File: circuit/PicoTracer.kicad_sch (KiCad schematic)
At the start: 19 parts, among them J1 Conn_01x04_Socket, J2 Conn_01x04_Socket, J3 Conn_01x04_Socket, J4 Conn_01x04_Socket, J5 Conn_01x04_Socket, J6 Conn_01x04_Socket, J7 8P8C, SW1 SW_Push, SW2 SW_Push, SW3 SW_Push, SW4 SW_SPDT, SW5 SW_SPDT, SW6 SW_SPDT, U1 Pico, U2 MCP3002, U3 MCP3002

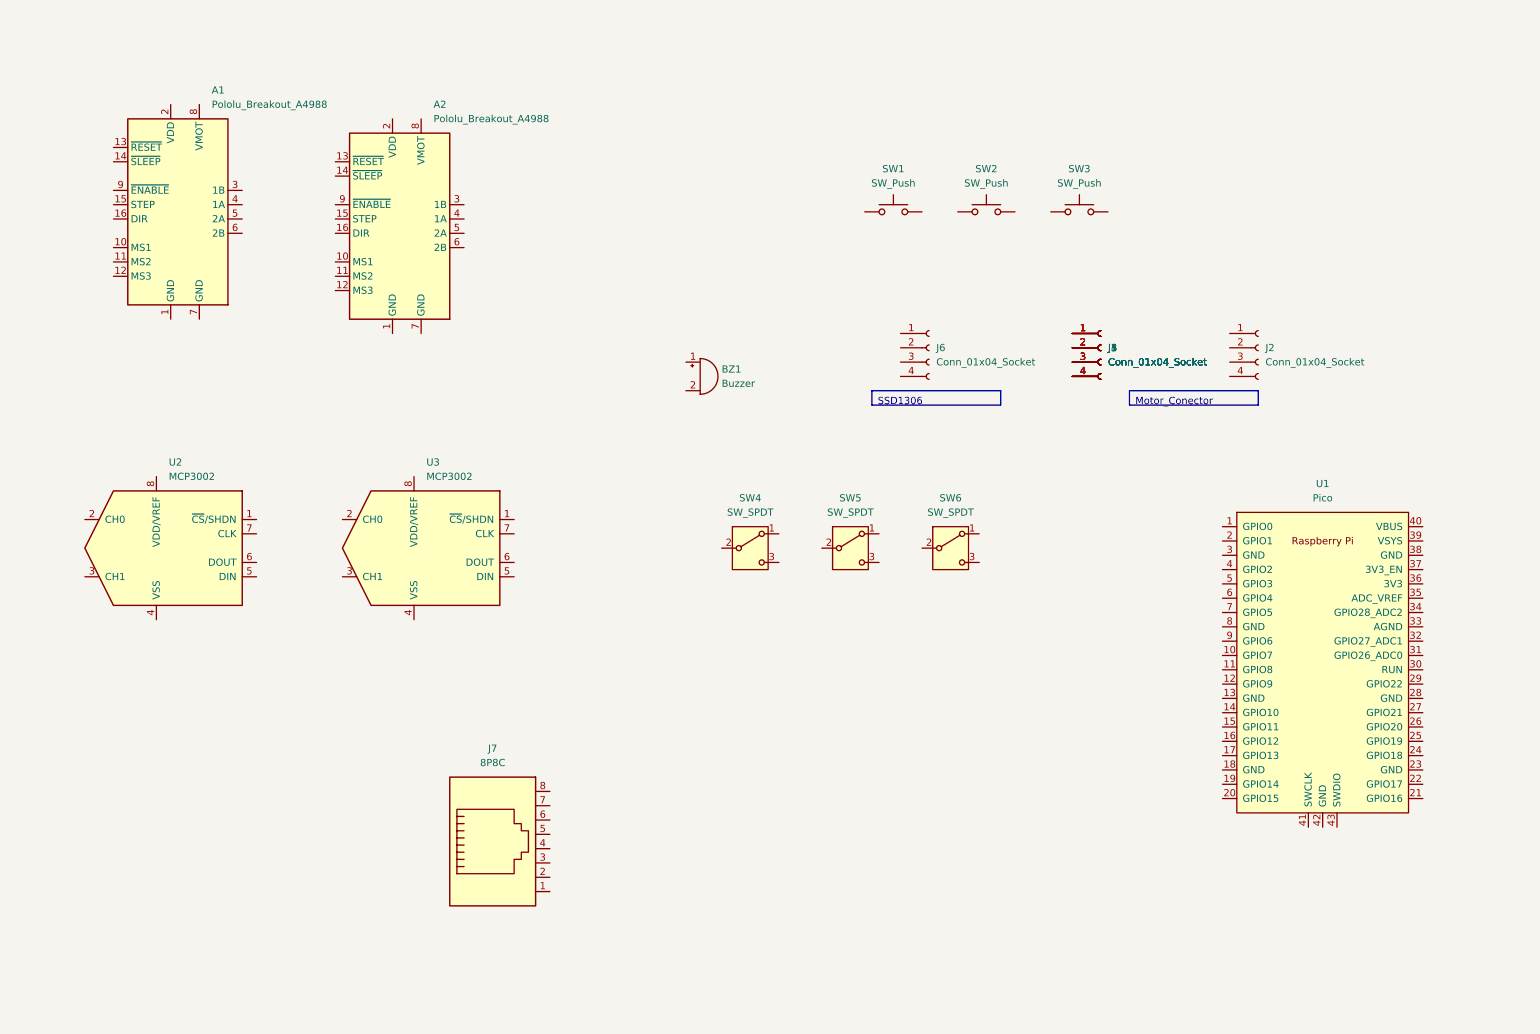
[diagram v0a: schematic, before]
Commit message: ・A4988の配線追加
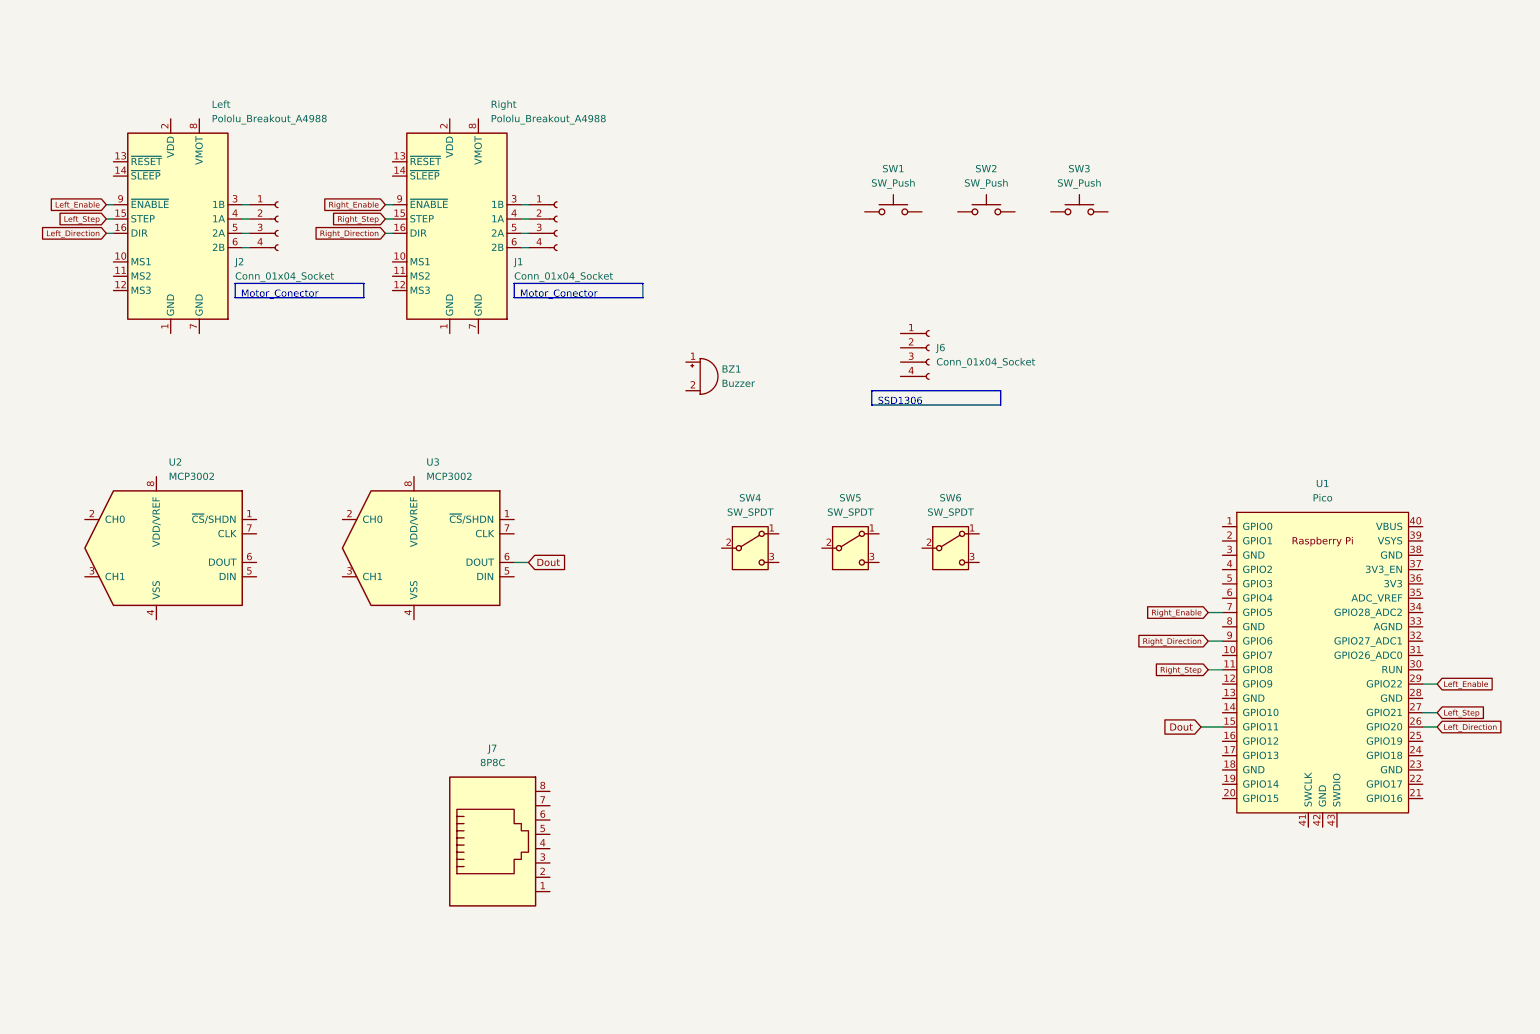
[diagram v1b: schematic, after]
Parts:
- removed J3, J4, J5: Conn_01x04_Socket, symbol Connector:Conn_01x04_Socket
- renumbered A1 to Left, A2 to Right
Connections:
- net at J1.1 (Pin_1): now also Right.3 (1B)
- net at J1.2 (Pin_2): now also Right.4 (1A)
- net at J1.3 (Pin_3): now also Right.5 (2A)
- net at J1.4 (Pin_4): now also Right.6 (2B)
- net at J2.1 (Pin_1): now also Left.3 (1B)
- net at J2.2 (Pin_2): now also Left.4 (1A)
- net at J2.3 (Pin_3): now also Left.5 (2A)
- net at J2.4 (Pin_4): now also Left.6 (2B)
- net Right_Step: now reaches U1.11 (GPIO8)
- net Right_Step: now also Right.15 (STEP)
- net Dout: now reaches U1.15 (GPIO11)
- net Dout: now also U3.6 (DOUT)
- net Left_Direction: now reaches U1.26 (GPIO20)
- net Left_Direction: now also Left.16 (DIR)
- net Left_Step: now reaches U1.27 (GPIO21)
- net Left_Step: now also Left.15 (STEP)
- net Left_Enable: now reaches U1.29 (GPIO22)
- net Left_Enable: now also Left.9 (~{ENABLE})
- net Right_Enable: now reaches U1.7 (GPIO5)
- net Right_Enable: now also Right.9 (~{ENABLE})
- net Right_Direction: now reaches U1.9 (GPIO6)
- net Right_Direction: now also Right.16 (DIR)
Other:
- moved on the sheet: J2, Left, Right

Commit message: ・スイッチ配線 ・AD変換器電源以外の配線完了
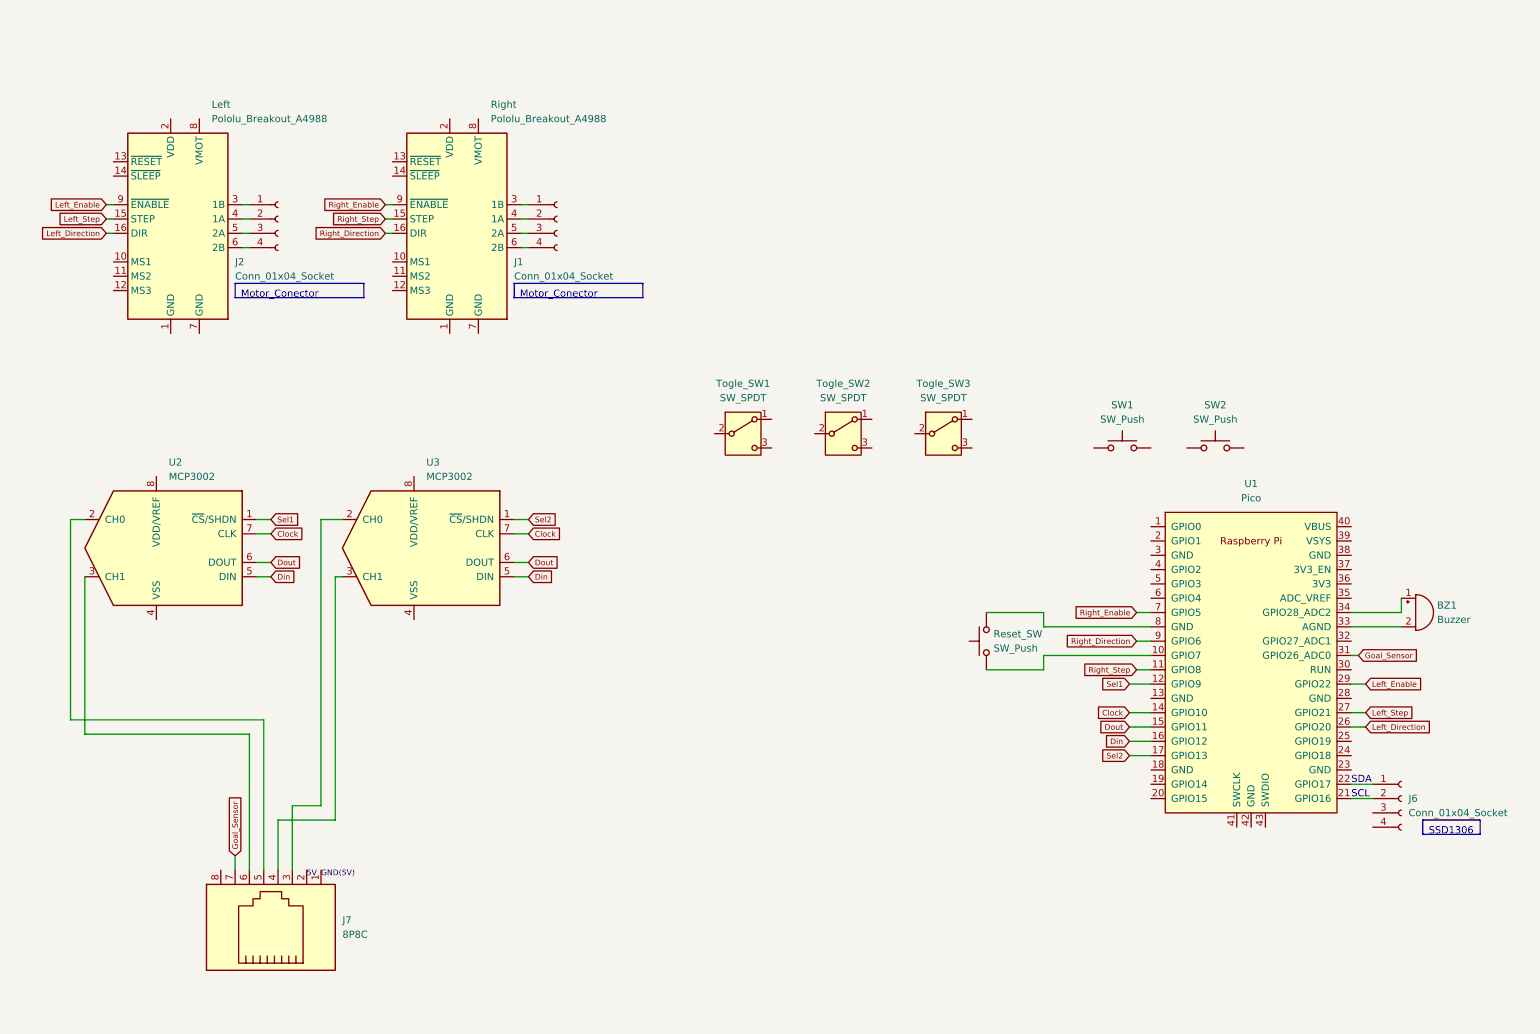
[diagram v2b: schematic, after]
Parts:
- renumbered SW3 to Reset_SW, SW4 to Togle_SW1, SW5 to Togle_SW2, SW6 to Togle_SW3
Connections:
- net Dout: now also U2.6 (DOUT)
- net at Reset_SW.1: now also U1.10 (GPIO7)
- net at Reset_SW.2: now also U1.8 (GND)
- net at J6.1 (Pin_1): now also U1.22 (GPIO17)
- net at J6.2 (Pin_2): now also U1.21 (GPIO16)
- net at J7.3: now also U3.2 (CH0)
- net at J7.4: now also U3.3 (CH1)
- net at J7.5: now also U2.2 (CH0)
- net at J7.6: now also U2.3 (CH1)
- net Goal_Sensor: now reaches J7.7
- net Goal_Sensor: now also U1.31 (GPIO26_ADC0)
- net Sel1: now reaches U2.1 (~{CS}/SHDN)
- net Sel1: now also U1.12 (GPIO9)
- net Din: now reaches U2.5 (DIN)
- net Din: now also U1.16 (GPIO12), U3.5 (DIN)
- net Clock: now reaches U2.7 (CLK)
- net Clock: now also U1.14 (GPIO10), U3.7 (CLK)
- net Sel2: now reaches U1.17 (GPIO13)
- net Sel2: now also U3.1 (~{CS}/SHDN)
- net at U1.33 (AGND): now also BZ1.2 (-)
- net at U1.34 (GPIO28_ADC2): now also BZ1.1 (+)
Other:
- note added: "5V"
- note added: "GND(5V)"
- note added: "SCL"
- note added: "SDA"
- moved on the sheet: BZ1, J6, J7, Reset_SW, SW1, SW2, Togle_SW1, Togle_SW2, Togle_SW3, U1

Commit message: scene5に電圧計測追加
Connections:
- net at Left.13 (~{RESET}): now also Left.14 (~{SLEEP})
- net at Right.13 (~{RESET}): now also Right.14 (~{SLEEP})
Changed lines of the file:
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@@
 (kicad_sch (version 20230121) (generator eeschema)
   (paper "A4")
+  (wire (pts (xy 34.29 43.18) (xy 34.29 45.72))
+    (stroke (width 0) (type default))
+  )
   (wire (pts (xy 63.5 160.02) (xy 63.5 168.91))
     (stroke (width 0) (type default))
@@
   )
   (wire (pts (xy 33.02 53.34) (xy 34.29 53.34))
+    (stroke (width 0) (type default))
+  )
+  (wire (pts (xy 83.82 43.18) (xy 83.82 45.72))
     (stroke (width 0) (type default))
   )
@@
     )
     (pin "1")
+    (pin "2")
+    (pin "3")
     (pin "4")
-    (pin "2")
-    (pin "3")
     (instances
       (project "PicoTracer"
@@
       (effects (font (size 1.27 1.27)) hide)
     )
-    (pin "2")
+    (pin "1")
+    (pin "2")
+    (pin "3")
     (pin "4")
-    (pin "3")
-    (pin "1")
     (instances
       (project "PicoTracer"
@@
       (effects (font (size 1.27 1.27)) hide)
     )
+    (pin "1")
+    (pin "2")
+    (pin "3")
+    (pin "4")
+    (pin "5")
+    (pin "6")
+    (pin "7")
     (pin "8")
+    (instances
+      (project "PicoTracer"
+        (path "/f79d951e-a1b3-4edf-883f-79f37eda87da"
+          (reference "J7") (unit 1)
+        )
+      )
+    )
+  )
+  (symbol (lib_id "Analog_ADC:MCP3002") (at 41.91 111.76 0) (unit 1)
+    (in_bom yes) (on_board yes) (dnp no) (fields_autoplaced)
+    (property "Reference" "U2" (at 44.1041 96.52 0)
+      (effects (font (size 1.27 1.27)) (justify left))
+    )
+    (property "Value" "MCP3002" (at 44.1041 99.06 0)
+      (effects (font (size 1.27 1.27)) (justify left))
+    )
+    (property "Footprint" "" (at 41.91 114.3 0)
+      (effects (font (size 1.27 1.27)) hide)
+    )
+    (property "Datasheet" "http://ww1.microchip.com/downloads/en/DeviceDoc/21294E.pdf" (at 41.91 106.68 0)
+      (effects (font (size 1.27 1.27)) hide)
+    )
+    (pin "1")
+    (pin "2")
+    (pin "3")
+    (pin "4")
+    (pin "5")
+    (pin "6")
     (pin "7")
-    (pin "5")
-    (pin "1")
-    (pin "4")
-    (pin "3")
-    (pin "6")
-    (pin "2")
-    (instances
-      (project "PicoTracer"
-        (path "/f79d951e-a1b3-4edf-883f-79f37eda87da"
-          (reference "J7") (unit 1)
-        )
-      )
-    )
-  )
-  (symbol (lib_id "Analog_ADC:MCP3002") (at 41.91 111.76 0) (unit 1)
-    (in_bom yes) (on_board yes) (dnp no) (fields_autoplaced)
-    (property "Reference" "U2" (at 44.1041 96.52 0)
-      (effects (font (size 1.27 1.27)) (justify left))
-    )
-    (property "Value" "MCP3002" (at 44.1041 99.06 0)
-      (effects (font (size 1.27 1.27)) (justify left))
-    )
-    (property "Footprint" "" (at 41.91 114.3 0)
-      (effects (font (size 1.27 1.27)) hide)
-    )
-    (property "Datasheet" "http://ww1.microchip.com/downloads/en/DeviceDoc/21294E.pdf" (at 41.91 106.68 0)
-      (effects (font (size 1.27 1.27)) hide)
-    )
-    (pin "6")
-    (pin "1")
-    (pin "2")
-    (pin "3")
-    (pin "5")
-    (pin "7")
-    (pin "4")
     (pin "8")
     (instances
@@
       (effects (font (size 1.27 1.27)) hide)
     )
-    (pin "15")
-    (pin "1")
+    (pin "1")
+    (pin "10")
+    (pin "11")
     (pin "12")
     (pin "13")
+    (pin "14")
+    (pin "15")
+    (pin "16")
+    (pin "17")
     (pin "18")
-    (pin "11")
-    (pin "10")
-    (pin "14")
-    (pin "17")
     (pin "19")
+    (pin "2")
     (pin "20")
     (pin "21")
     (pin "22")
     (pin "23")
-    (pin "2")
-    (pin "16")
     (pin "24")
-    (pin "5")
-    (pin "6")
-    (pin "4")
+    (pin "25")
+    (pin "26")
+    (pin "27")
+    (pin "28")
+    (pin "29")
+    (pin "3")
+    (pin "30")
+    (pin "31")
+    (pin "32")
+    (pin "33")
+    (pin "34")
+    (pin "35")
+    (pin "36")
+    (pin "37")
     (pin "38")
     (pin "39")
-    (pin "8")
-    (pin "9")
-    (pin "3")
-    (pin "7")
+    (pin "4")
     (pin "40")
-    (pin "36")
-    (pin "30")
-    (pin "35")
-    (pin "29")
-    (pin "26")
-    (pin "28")
-    (pin "32")
-    (pin "34")
     (pin "41")
     (pin "42")
     (pin "43")
-    (pin "27")
-    (pin "25")
-    (pin "37")
-    (pin "33")
-    (pin "31")
+    (pin "5")
+    (pin "6")
+    (pin "7")
+    (pin "8")
+    (pin "9")
     (instances
       (project "PicoTracer"
@@
       (effects (font (size 1.27 1.27)) hide)
     )
-    (pin "2")
-    (pin "1")
+    (pin "1")
+    (pin "2")
     (instances
       (project "PicoTracer"
@@
       (effects (font (size 1.27 1.27)) hide)
     )
+    (pin "1")
+    (pin "10")
+    (pin "11")
     (pin "12")
     (pin "13")
+    (pin "14")
     (pin "15")
-    (pin "2")
-    (pin "1")
-    (pin "10")
-    (pin "11")
-    (pin "14")
     (pin "16")
-    (pin "3")
+    (pin "2")
+    (pin "3")
+    (pin "4")
     (pin "5")
     (pin "6")
+    (pin "7")
     (pin "8")
     (pin "9")
-    (pin "7")
-    (pin "4")
     (instances
       (project "PicoTracer"
@@
       (effects (font (size 1.27 1.27)) hide)
     )
+    (pin "1")
+    (pin "10")
+    (pin "11")
     (pin "12")
     (pin "13")
+    (pin "14")
     (pin "15")
-    (pin "2")
-    (pin "1")
-    (pin "10")
-    (pin "11")
-    (pin "14")
     (pin "16")
-    (pin "3")
+    (pin "2")
+    (pin "3")
+    (pin "4")
     (pin "5")
     (pin "6")
+    (pin "7")
     (pin "8")
     (pin "9")
+    (instances
+      (project "PicoTracer"
+        (path "/f79d951e-a1b3-4edf-883f-79f37eda87da"
+          (reference "Right") (unit 1)
+        )
+      )
+    )
+  )
+  (symbol (lib_id "Switch:SW_Push") (at 213.36 93.98 0) (unit 1)
+    (in_bom yes) (on_board yes) (dnp no) (fields_autoplaced)
+    (property "Reference" "SW1" (at 213.36 86.36 0)
+      (effects (font (size 1.27 1.27)))
+    )
+    (property "Value" "SW_Push" (at 213.36 88.9 0)
+      (effects (font (size 1.27 1.27)))
+    )
+    (property "Footprint" "" (at 213.36 88.9 0)
+      (effects (font (size 1.27 1.27)) hide)
+    )
+    (property "Datasheet" "~" (at 213.36 88.9 0)
+      (effects (font (size 1.27 1.27)) hide)
+    )
+    (pin "1")
+    (pin "2")
+    (instances
+      (project "PicoTracer"
+        (path "/f79d951e-a1b3-4edf-883f-79f37eda87da"
+          (reference "SW1") (unit 1)
+        )
+      )
+    )
+  )
+  (symbol (lib_id "Analog_ADC:MCP3002") (at 87.63 111.76 0) (unit 1)
+    (in_bom yes) (on_board yes) (dnp no) (fields_autoplaced)
+    (property "Reference" "U3" (at 89.8241 96.52 0)
+      (effects (font (size 1.27 1.27)) (justify left))
+    )
+    (property "Value" "MCP3002" (at 89.8241 99.06 0)
+      (effects (font (size 1.27 1.27)) (justify left))
+    )
+    (property "Footprint" "" (at 87.63 114.3 0)
+      (effects (font (size 1.27 1.27)) hide)
+    )
+    (property "Datasheet" "http://ww1.microchip.com/downloads/en/DeviceDoc/21294E.pdf" (at 87.63 106.68 0)
+      (effects (font (size 1.27 1.27)) hide)
+    )
+    (pin "1")
+    (pin "2")
+    (pin "3")
+    (pin "4")
+    (pin "5")
+    (pin "6")
     (pin "7")
-    (pin "4")
-    (instances
-      (project "PicoTracer"
-        (path "/f79d951e-a1b3-4edf-883f-79f37eda87da"
-          (reference "Right") (unit 1)
-        )
-      )
-    )
-  )
-  (symbol (lib_id "Switch:SW_Push") (at 213.36 93.98 0) (unit 1)
-    (in_bom yes) (on_board yes) (dnp no) (fields_autoplaced)
-    (property "Reference" "SW1" (at 213.36 86.36 0)
-      (effects (font (size 1.27 1.27)))
-    )
-    (property "Value" "SW_Push" (at 213.36 88.9 0)
-      (effects (font (size 1.27 1.27)))
-    )
-    (property "Footprint" "" (at 213.36 88.9 0)
-      (effects (font (size 1.27 1.27)) hide)
-    )
-    (property "Datasheet" "~" (at 213.36 88.9 0)
-      (effects (font (size 1.27 1.27)) hide)
-    )
-    (pin "1")
-    (pin "2")
-    (instances
-      (project "PicoTracer"
-        (path "/f79d951e-a1b3-4edf-883f-79f37eda87da"
-          (reference "SW1") (unit 1)
-        )
-      )
-    )
-  )
-  (symbol (lib_id "Analog_ADC:MCP3002") (at 87.63 111.76 0) (unit 1)
-    (in_bom yes) (on_board yes) (dnp no) (fields_autoplaced)
-    (property "Reference" "U3" (at 89.8241 96.52 0)
-      (effects (font (size 1.27 1.27)) (justify left))
-    )
-    (property "Value" "MCP3002" (at 89.8241 99.06 0)
-      (effects (font (size 1.27 1.27)) (justify left))
-    )
-    (property "Footprint" "" (at 87.63 114.3 0)
-      (effects (font (size 1.27 1.27)) hide)
-    )
-    (property "Datasheet" "http://ww1.microchip.com/downloads/en/DeviceDoc/21294E.pdf" (at 87.63 106.68 0)
-      (effects (font (size 1.27 1.27)) hide)
-    )
-    (pin "6")
-    (pin "1")
-    (pin "2")
-    (pin "3")
-    (pin "5")
-    (pin "7")
-    (pin "4")
     (pin "8")
     (instances
@@
     )
     (pin "1")
+    (pin "2")
+    (pin "3")
     (pin "4")
-    (pin "2")
-    (pin "3")
-    (instances
-      (project "PicoTracer"
+    (instances
+      (project "PicoTracer"
